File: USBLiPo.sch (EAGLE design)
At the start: 15 parts, among them IC1 LTC4054, Q1 2N7002 SOT-23

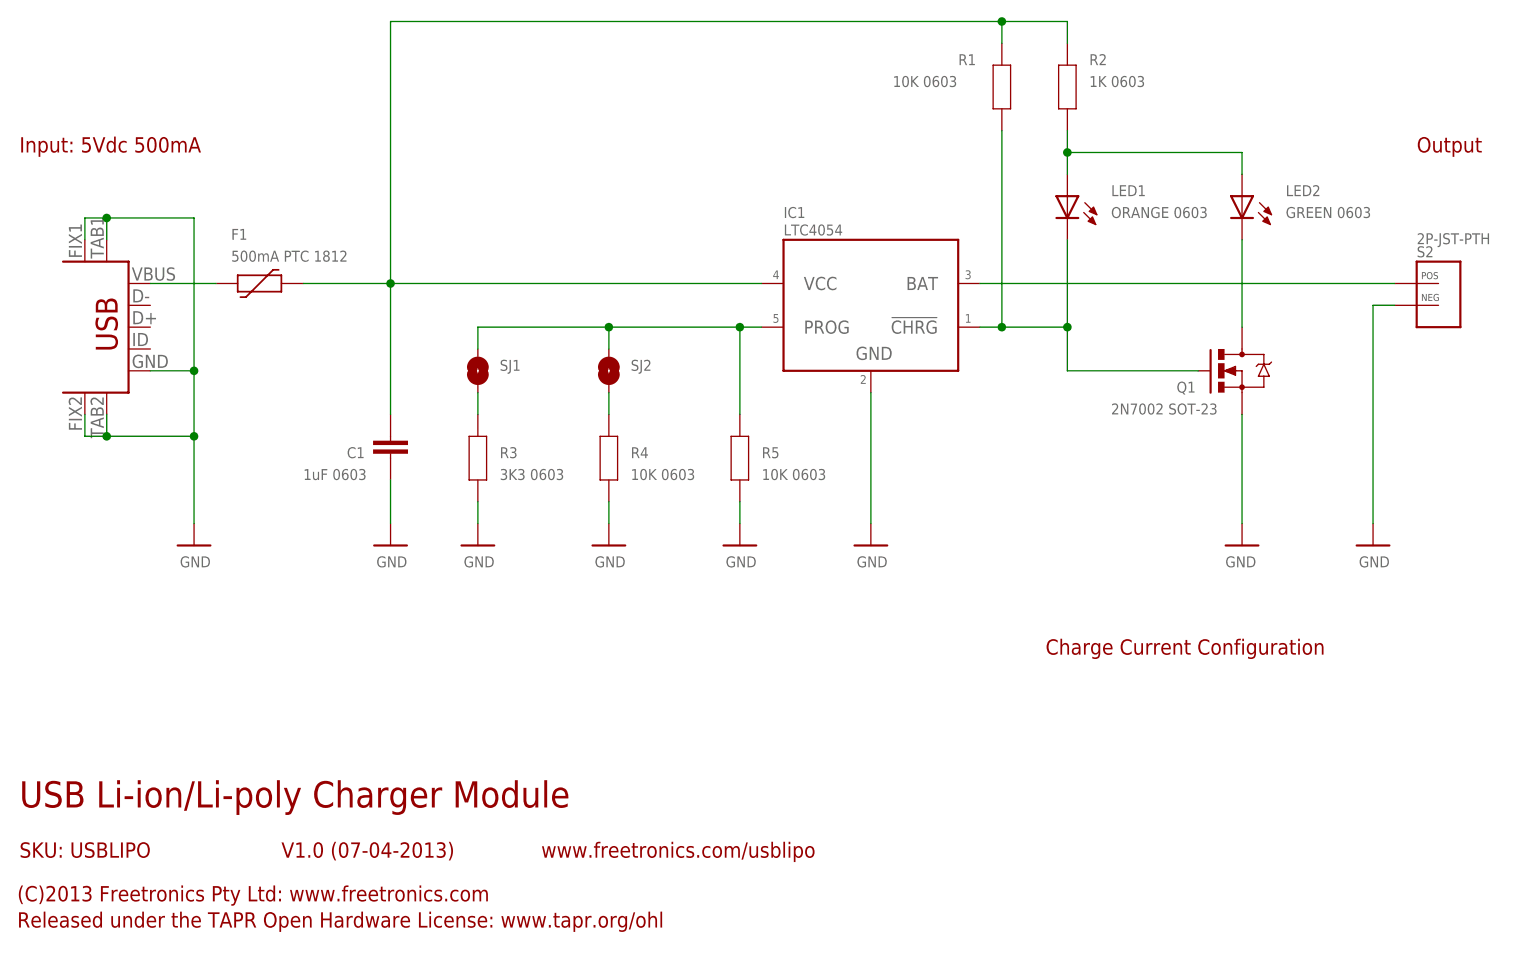
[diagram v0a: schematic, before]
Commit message: Changed USB socket to strong footprint; added 0.1 battery connector
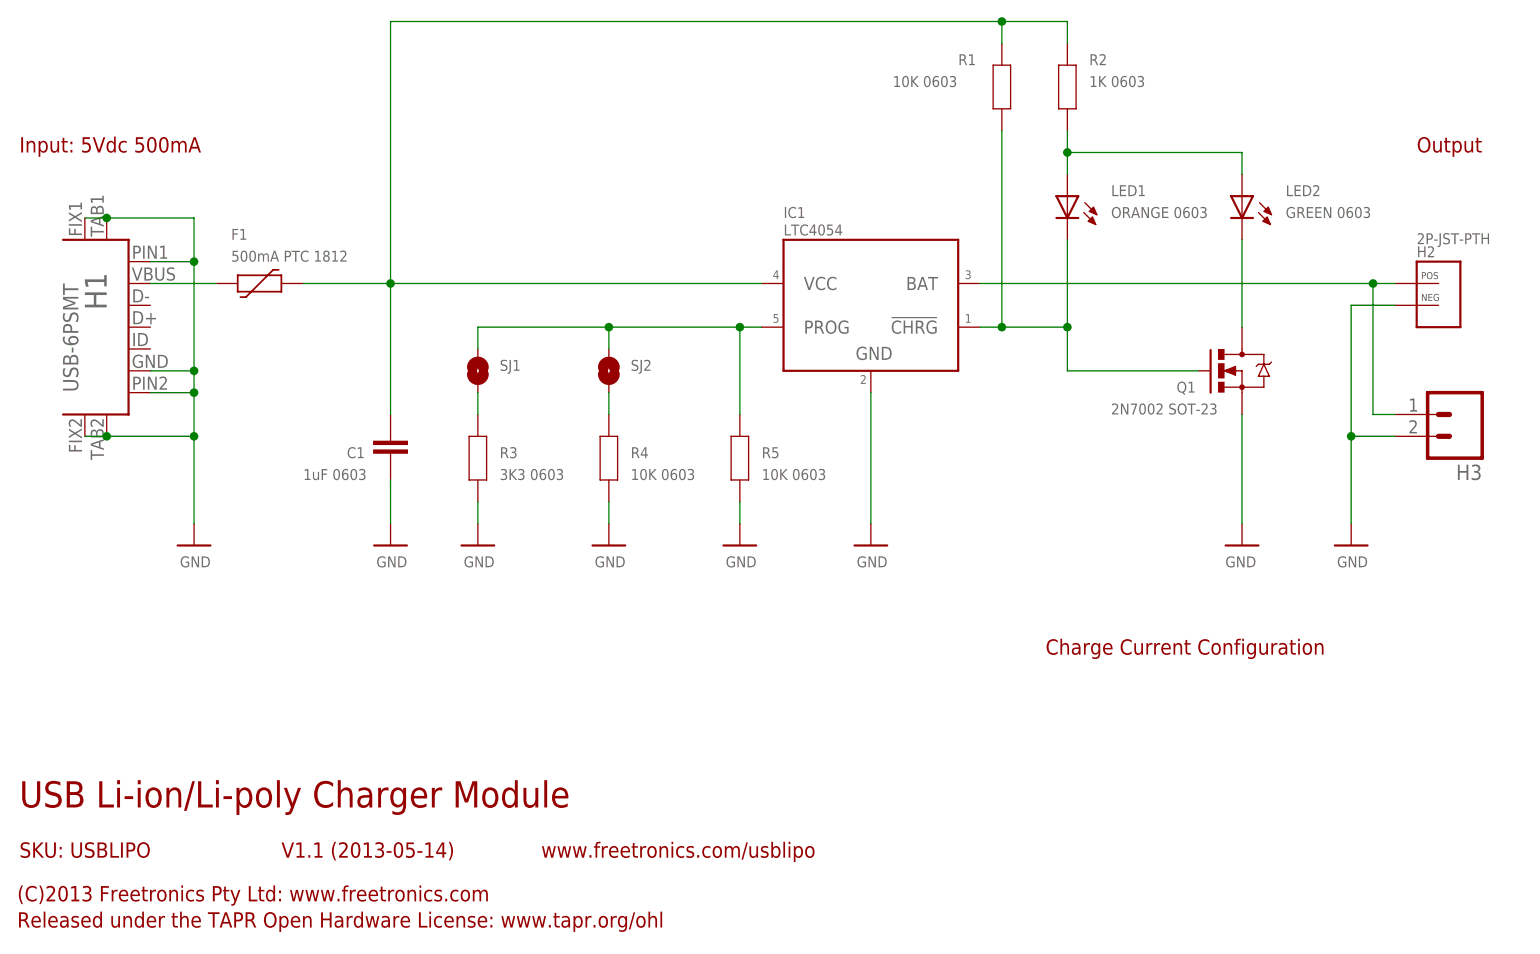
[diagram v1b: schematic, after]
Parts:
- removed S1: USBSF-MICROB, freetronics-jon:USBSF-MICROB
- added H1: USB-6PSMT, freetronics-jon:USB-6PSMT
- added H3: (no value), freetronics-master-v1.1:M02PTH
- renumbered S2 to H2
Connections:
- net GND: now also H1.FIX1, H1.FIX2, H1.GND, H1.PIN1, H1.PIN2, H1.TAB1, H1.TAB2, H3.2; no longer S1.FIX1, S1.FIX2, S1.GND, S1.TAB1, S1.TAB2
- net N$113: now also H1.VBUS; no longer S1.VBUS
- net N$4: now also H3.1
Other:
- note added: "V1.1 (2013-05-14)"
- note removed: "V1.0 (07-04-2013)"
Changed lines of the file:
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@@
 <part name="SJ1" library="freetronics-luke" deviceset="SJ" device=""/>
 <part name="SJ2" library="freetronics-luke" deviceset="SJ" device=""/>
-<part name="S2" library="freetronics-jon" deviceset="FREETRONICS-LUKE_2P-JST-TH-RA" device="PTH" value="2P-JST-PTH"/>
+<part name="H2" library="freetronics-jon" deviceset="FREETRONICS-LUKE_2P-JST-TH-RA" device="PTH" value="2P-JST-PTH"/>
 <part name="U$9" library="freetronics-luke" deviceset="GND" device=""/>
-<part name="S1" library="freetronics-jon" deviceset="USBSF" device="-MICROB"/>
+<part name="H1" library="freetronics-jon" deviceset="USB-6P" device="SMT"/>
+<part name="H3" library="freetronics-master-v1.1" deviceset="M02" device="PTH"/>
 </parts>
 <sheets>
@@
 <plain>
 <text x="7.62" y="20.32" size="3.048" layer="94">USB Li-ion/Li-poly Charger Module</text>
-<text x="38.1" y="14.478" size="1.778" layer="94">V1.0 (07-04-2013)</text>
+<text x="38.1" y="14.478" size="1.778" layer="94">V1.1 (2013-05-14)</text>
 <text x="7.62" y="14.478" size="1.778" layer="94">SKU: USBLIPO</text>
 <text x="7.366" y="9.398" size="1.778" layer="94">(C)2013 Freetronics Pty Ltd: www.freetronics.com</text>
@@
 <attribute name="NAME" x="78.74" y="71.12" size="1.27" layer="95"/>
 </instance>
-<instance part="S2" gate="G$1" x="170.18" y="78.74"/>
-<instance part="U$9" gate="G$1" x="165.1" y="50.8"/>
-<instance part="S1" gate="G$1" x="17.78" y="76.2" rot="R180"/>
+<instance part="H2" gate="G$1" x="170.18" y="78.74"/>
+<instance part="U$9" gate="G$1" x="162.56" y="50.8"/>
+<instance part="H1" gate="G$1" x="17.78" y="76.2" rot="R180"/>
+<instance part="H3" gate="G$1" x="175.26" y="66.04" rot="R180"/>
 </instances>
 <busses>
@@
 <segment>
 <wire x1="22.86" y1="71.12" x2="27.94" y2="71.12" width="0.1524" layer="91"/>
-<wire x1="27.94" y1="71.12" x2="27.94" y2="63.5" width="0.1524" layer="91"/>
+<wire x1="27.94" y1="71.12" x2="27.94" y2="68.58" width="0.1524" layer="91"/>
+<wire x1="27.94" y1="68.58" x2="27.94" y2="63.5" width="0.1524" layer="91"/>
 <wire x1="27.94" y1="63.5" x2="27.94" y2="53.34" width="0.1524" layer="91"/>
 <wire x1="27.94" y1="63.5" x2="17.78" y2="63.5" width="0.1524" layer="91"/>
-<wire x1="17.78" y1="63.5" x2="17.78" y2="66.04" width="0.1524" layer="91"/>
 <junction x="27.94" y="63.5"/>
 <pinref part="U$2" gate="G$1" pin="GND"/>
-<pinref part="S1" gate="G$1" pin="TAB2"/>
-<pinref part="S1" gate="G$1" pin="GND"/>
-<pinref part="S1" gate="G$1" pin="TAB1"/>
-<wire x1="17.78" y1="86.36" x2="17.78" y2="88.9" width="0.1524" layer="91"/>
+<pinref part="H1" gate="G$1" pin="TAB2"/>
+<pinref part="H1" gate="G$1" pin="GND"/>
+<pinref part="H1" gate="G$1" pin="TAB1"/>
 <wire x1="17.78" y1="88.9" x2="27.94" y2="88.9" width="0.1524" layer="91"/>
-<wire x1="27.94" y1="88.9" x2="27.94" y2="71.12" width="0.1524" layer="91"/>
+<wire x1="27.94" y1="88.9" x2="27.94" y2="83.82" width="0.1524" layer="91"/>
 <junction x="27.94" y="71.12"/>
-<pinref part="S1" gate="G$1" pin="FIX1"/>
-<wire x1="15.24" y1="86.36" x2="15.24" y2="88.9" width="0.1524" layer="91"/>
+<pinref part="H1" gate="G$1" pin="FIX1"/>
+<wire x1="27.94" y1="83.82" x2="27.94" y2="71.12" width="0.1524" layer="91"/>
 <wire x1="15.24" y1="88.9" x2="17.78" y2="88.9" width="0.1524" layer="91"/>
-<pinref part="S1" gate="G$1" pin="FIX2"/>
-<wire x1="15.24" y1="66.04" x2="15.24" y2="63.5" width="0.1524" layer="91"/>
+<pinref part="H1" gate="G$1" pin="FIX2"/>
 <wire x1="15.24" y1="63.5" x2="17.78" y2="63.5" width="0.1524" layer="91"/>
 <junction x="17.78" y="63.5"/>
 <junction x="17.78" y="88.9"/>
+<pinref part="H1" gate="G$1" pin="PIN1"/>
+<wire x1="22.86" y1="83.82" x2="27.94" y2="83.82" width="0.1524" layer="91"/>
+<pinref part="H1" gate="G$1" pin="PIN2"/>
+<wire x1="22.86" y1="68.58" x2="27.94" y2="68.58" width="0.1524" layer="91"/>
+<junction x="27.94" y="68.58"/>
+<junction x="27.94" y="83.82"/>
 </segment>
 <segment>
@@
 </segment>
 <segment>
-<pinref part="S2" gate="G$1" pin="NEG"/>
-<wire x1="167.64" y1="78.74" x2="165.1" y2="78.74" width="0.1524" layer="91"/>
-<wire x1="165.1" y1="78.74" x2="165.1" y2="53.34" width="0.1524" layer="91"/>
+<pinref part="H2" gate="G$1" pin="NEG"/>
+<wire x1="167.64" y1="78.74" x2="162.56" y2="78.74" width="0.1524" layer="91"/>
+<wire x1="162.56" y1="78.74" x2="162.56" y2="63.5" width="0.1524" layer="91"/>
 <pinref part="U$9" gate="G$1" pin="GND"/>
+<pinref part="H3" gate="G$1" pin="2"/>
+<wire x1="162.56" y1="63.5" x2="162.56" y2="53.34" width="0.1524" layer="91"/>
+<wire x1="167.64" y1="63.5" x2="162.56" y2="63.5" width="0.1524" layer="91"/>
+<junction x="162.56" y="63.5"/>
 </segment>
 </net>
@@
 <wire x1="22.86" y1="81.28" x2="30.48" y2="81.28" width="0.1524" layer="91"/>
 <pinref part="F1" gate="G$1" pin="P$1"/>
-<pinref part="S1" gate="G$1" pin="VBUS"/>
+<pinref part="H1" gate="G$1" pin="VBUS"/>
 </segment>
 </net>
@@
 <segment>
 <pinref part="IC1" gate="G$1" pin="BAT"/>
-<pinref part="S2" gate="G$1" pin="POS"/>
-<wire x1="119.38" y1="81.28" x2="167.64" y2="81.28" width="0.1524" layer="91"/>
-</segment>
-</net>
+<pinref part="H2" gate="G$1" pin="POS"/>
+<wire x1="119.38" y1="81.28" x2="165.1" y2="81.28" width="0.1524" layer="91"/>
+<pinref part="H3" gate="G$1" pin="1"/>
+<wire x1="165.1" y1="81.28" x2="167.64" y2="81.28" width="0.1524" layer="91"/>
+<wire x1="167.64" y1="66.04" x2="165.1" y2="66.04" width="0.1524" layer="91"/>
+<wire x1="165.1" y1="66.04" x2="165.1" y2="81.28" width="0.1524" layer="91"/>
+<junction x="165.1" y="81.28"/>
+</segment>
+</net>

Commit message: Switched pads to bottom; shorter board; ready for v1.1 release
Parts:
- H2: device freetronics-jon:FREETRONICS-LUKE_2P-JST-TH-RAPTH -> freetronics-jon:2P-JST-TH-RAPTH
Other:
- note added: "V1.1 (2013-05-15)"
- note removed: "V1.1 (2013-05-14)"
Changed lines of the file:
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@@
 <part name="SJ1" library="freetronics-luke" deviceset="SJ" device=""/>
 <part name="SJ2" library="freetronics-luke" deviceset="SJ" device=""/>
-<part name="H2" library="freetronics-jon" deviceset="FREETRONICS-LUKE_2P-JST-TH-RA" device="PTH" value="2P-JST-PTH"/>
+<part name="H2" library="freetronics-jon" deviceset="2P-JST-TH-RA" device="PTH" value="2P-JST-PTH"/>
 <part name="U$9" library="freetronics-luke" deviceset="GND" device=""/>
 <part name="H1" library="freetronics-jon" deviceset="USB-6P" device="SMT"/>
@@
 <plain>
 <text x="7.62" y="20.32" size="3.048" layer="94">USB Li-ion/Li-poly Charger Module</text>
-<text x="38.1" y="14.478" size="1.778" layer="94">V1.1 (2013-05-14)</text>
+<text x="38.1" y="14.478" size="1.778" layer="94">V1.1 (2013-05-15)</text>
 <text x="7.62" y="14.478" size="1.778" layer="94">SKU: USBLIPO</text>
 <text x="7.366" y="9.398" size="1.778" layer="94">(C)2013 Freetronics Pty Ltd: www.freetronics.com</text>

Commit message: Fix silkscreen error, one charge current setting was wrong Bump version to 1.2.
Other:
- note added: "V1.2 (2015-03-05)"
- note removed: "V1.1 (2013-05-15)"
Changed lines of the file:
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@@
 <?xml version="1.0" encoding="utf-8"?>
 <!DOCTYPE eagle SYSTEM "eagle.dtd">
-<eagle version="6.3">
+<eagle version="6.5.0">
 <drawing>
 <settings>
@@
 <plain>
 <text x="7.62" y="20.32" size="3.048" layer="94">USB Li-ion/Li-poly Charger Module</text>
-<text x="38.1" y="14.478" size="1.778" layer="94">V1.1 (2013-05-15)</text>
+<text x="38.1" y="14.478" size="1.778" layer="94">V1.2 (2015-03-05)</text>
 <text x="7.62" y="14.478" size="1.778" layer="94">SKU: USBLIPO</text>
 <text x="7.366" y="9.398" size="1.778" layer="94">(C)2013 Freetronics Pty Ltd: www.freetronics.com</text>
